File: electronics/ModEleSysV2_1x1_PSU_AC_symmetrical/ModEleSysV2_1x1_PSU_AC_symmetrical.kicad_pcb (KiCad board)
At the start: 2 copper layers, 43.2 x 49.5 mm, 29 parts, among them J2 Jack-DC, SW1 switch_DPDT, U1 LM317, U2 LM337

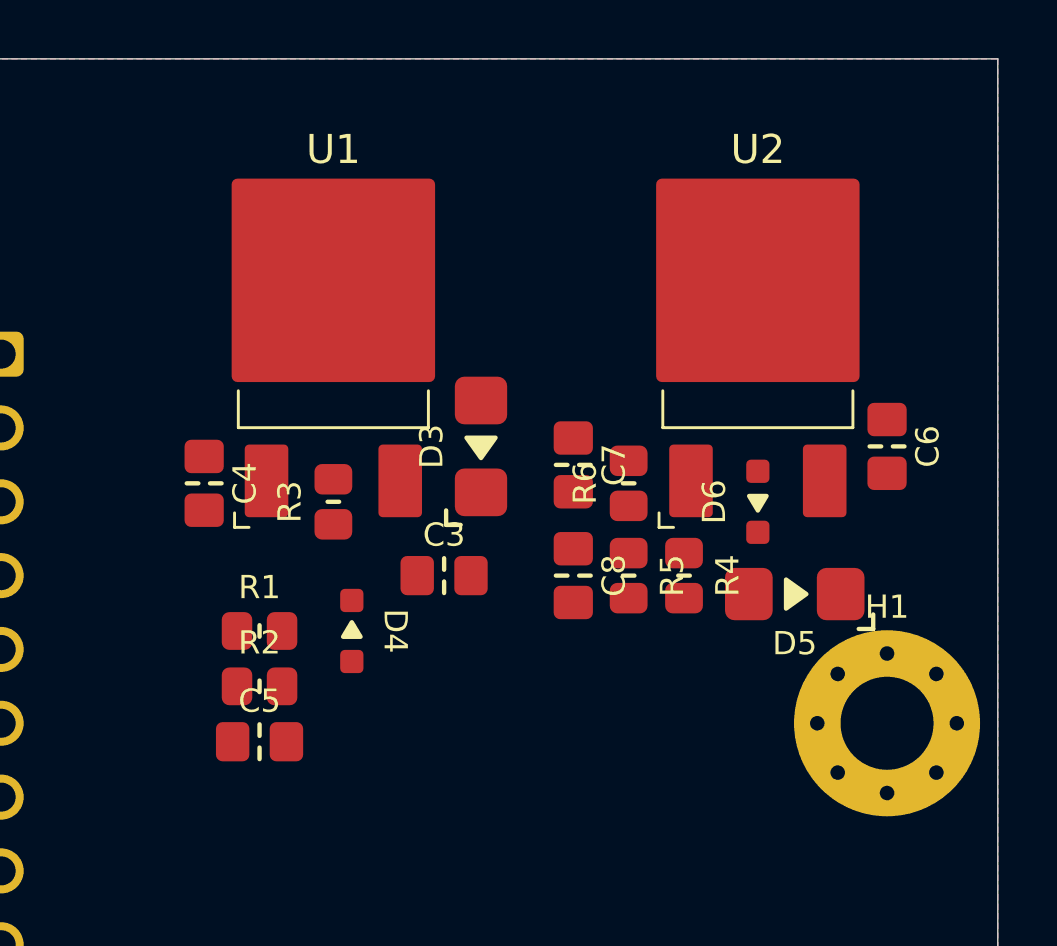
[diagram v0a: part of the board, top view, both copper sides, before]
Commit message: WIP placement of parts and reducing sizes, it is a bit cramped
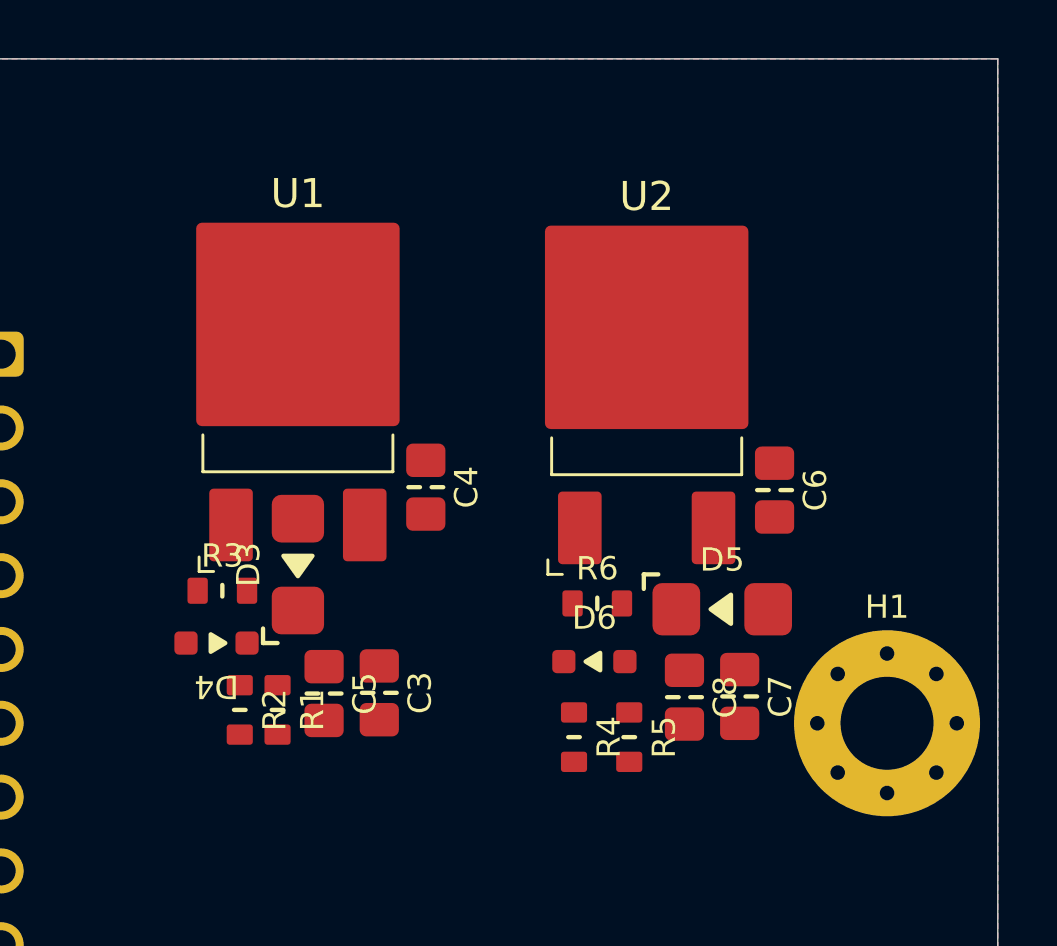
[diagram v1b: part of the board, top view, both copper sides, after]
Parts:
- R1, R2, R3, R4, R5, R6: footprint SquantorResistor:R_0805+0603 -> SquantorResistor:R_0603_hand
- moved C7 9.81 mm to (174.0, 85.4)
- moved D6 7.87 mm to (169.0, 84.2), turned to 0 degrees
- moved C4 7.63 mm to (163.2, 78.2)
- moved D3 7.50 mm to (158.8, 80.9)
- moved R4 6.72 mm to (168.3, 86.8)
- moved C8 5.67 mm to (172.1, 85.5)
- moved R5 5.56 mm to (170.2, 86.8)
- moved R3 4.89 mm to (156.2, 81.8), turned to 0 degrees
- moved D4 4.67 mm to (156.0, 83.6), turned to 180 degrees
- moved C3 4.61 mm to (161.6, 85.3), turned to -90 degrees
- moved R6 4.27 mm to (169.1, 82.2), turned to 0 degrees
- moved U2 4.15 mm to (170.8, 72.7)
- moved C6 4.15 mm to (175.2, 78.3)
- moved R1 2.78 mm to (158.1, 85.9), turned to -90 degrees
- moved C5 2.77 mm to (159.7, 85.3), turned to -90 degrees
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
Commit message: done, needs review in between
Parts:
- added C9: 10n, SquantorCapacitor:C_0805+0603, F.Cu at (150.0, 106.9)
- D1, D2: value D -> A7
- D3, D5: value D -> B5819WS; footprint SquantorDiodes:SOD-123F-hand -> SquantorDiodes:SOD-323HE-shikues
- D4, D6: value D -> B5819WS; footprint SquantorDiodes:SOD-323-nexperia-hand -> SquantorDiodes:SOD-323HE-shikues
- F1: value Fuse -> 0.6A 60V
- R1, R2, R4, R5: value R -> TBD
- moved R4 24.5 mm to (180.2, 65.5), turned to 90 degrees
- moved R5 23.1 mm to (178.9, 65.5), turned to 90 degrees
- moved C8 20.9 mm to (176.5, 65.0), turned to 180 degrees
- moved D6 19.2 mm to (179.0, 67.8), turned to 180 degrees
- moved C7 16.8 mm to (174.1, 68.6), turned to 180 degrees
- moved R6 16.4 mm to (179.5, 69.5), turned to 180 degrees
- moved D5 11.6 mm to (177.1, 71.5), turned to -90 degrees
- moved U2 8.82 mm to (177.1, 78.9), turned to 180 degrees
- moved C3 8.82 mm to (170.4, 85.9)
- moved D4 8.27 mm to (164.0, 85.7)
- moved C4 7.95 mm to (170.4, 81.6)
- moved R3 7.72 mm to (163.6, 84.0)
- moved U1 7.53 mm to (166.0, 74.8)
- moved C5 7.37 mm to (166.9, 86.9), turned to 90 degrees
- moved D3 7.33 mm to (166.0, 82.3)
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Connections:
- net Net-(D4-A) renamed /+adj
- net Net-(D6-K) renamed /-adj
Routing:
- net /+aV: track 0.00 -> 45.2 mm, vias 0 -> 15
- net /-aV: track 0.00 -> 42.8 mm
- net GND: track 0.00 -> 37.3 mm, vias 0 -> 12
- net /DC1n: track 0.00 -> 35.0 mm, vias 0 -> 14
- net /DC1p: track 0.00 -> 29.7 mm
- net /AC_PHASE1_IN: track 0.00 -> 16.4 mm
- net Net-(SW1-SW1_C1): track 0.00 -> 11.4 mm
- net /+adj: track 0.00 -> 10.5 mm
- net /-adj: track 0.00 -> 10.3 mm
- net /AC_NEUT_IN: track 0.00 -> 10.2 mm
- net /AC1_PHASE: track 0.00 -> 8.13 mm
- added copper zone on B.Cu, net /+aV
- added copper zone on F.Cu, net /+aV
- added copper zone on F.Cu, net /-aV
- added copper zone on F.Cu, net /AC1_PHASE
- added copper zone on B.Cu, net /DC1n
- added copper zone on F.Cu, net /DC1n
- added copper zone on F.Cu, net /DC1p

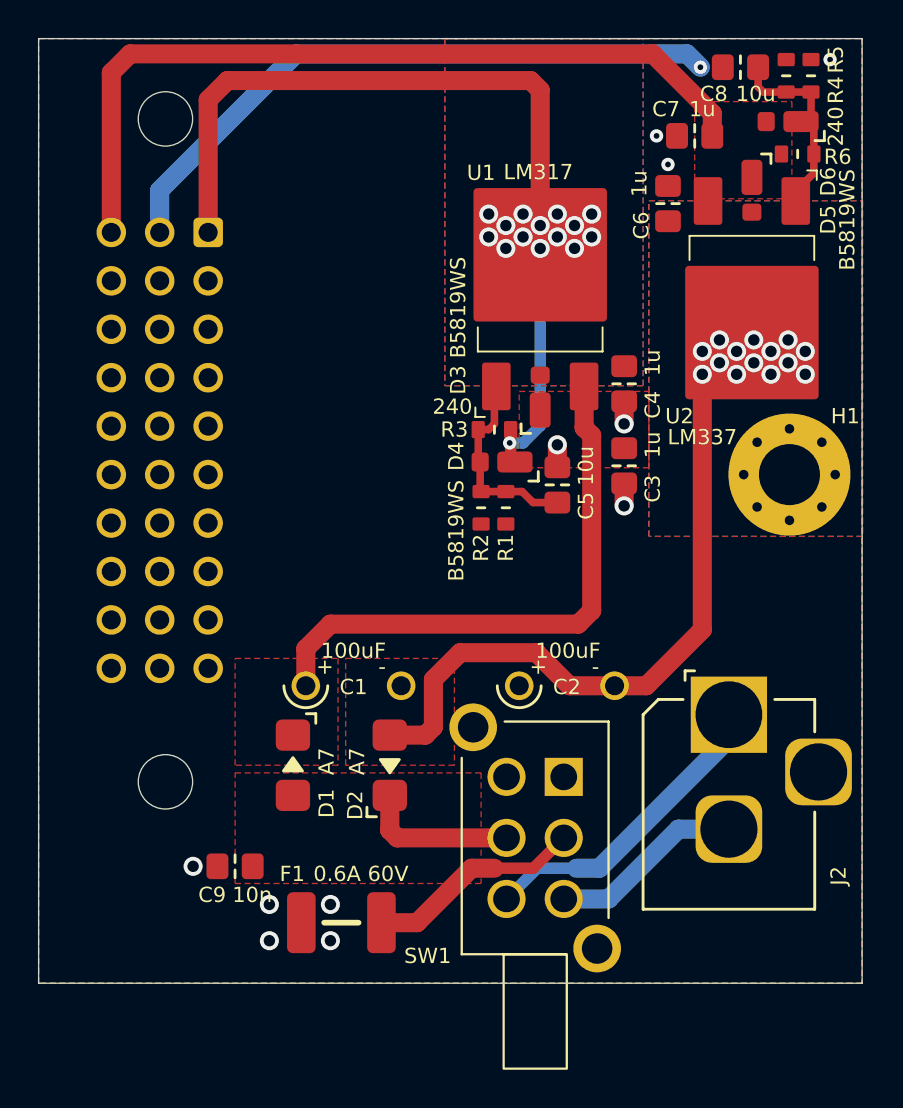
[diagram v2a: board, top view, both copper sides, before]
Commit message: reviewed and different placement of switch and power input
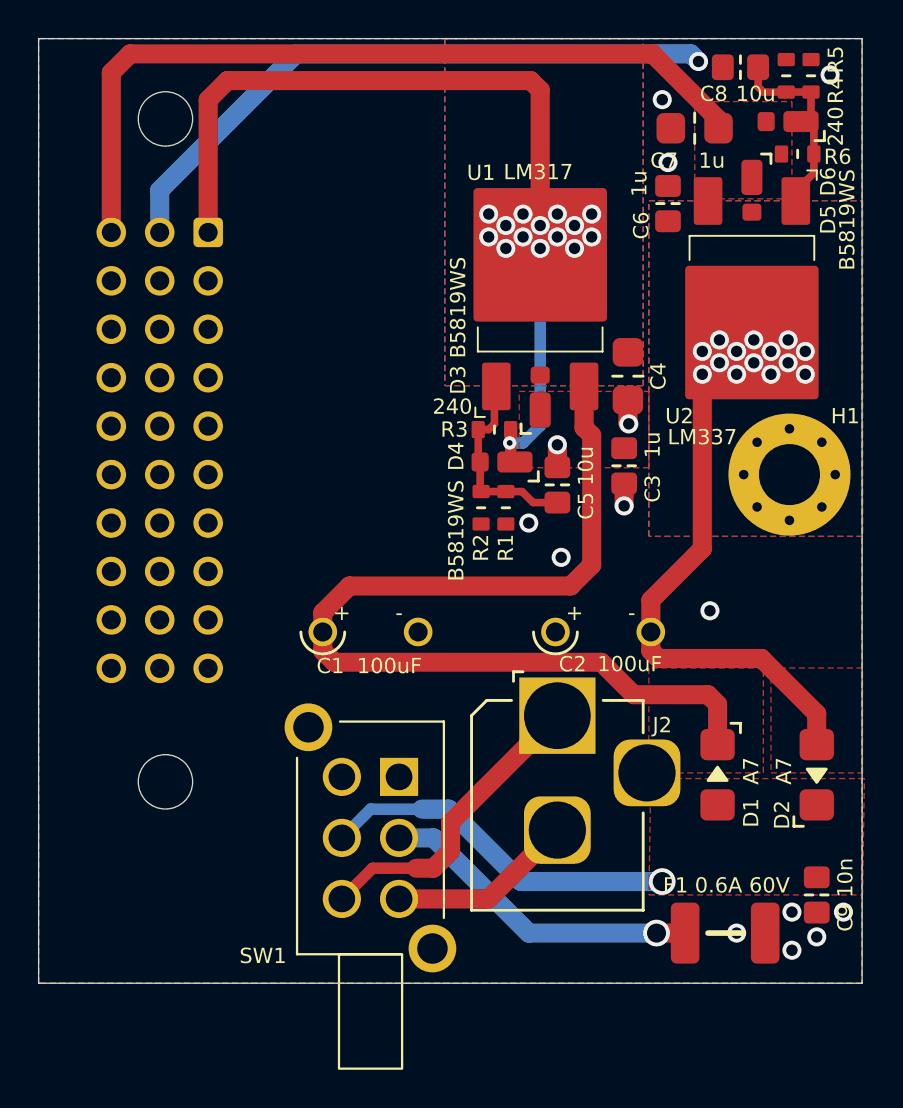
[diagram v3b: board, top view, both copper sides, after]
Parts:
- C4, C7: footprint SquantorCapacitor:C_0805+0603 -> SquantorCapacitor:C_1206_0805
- N1: value 20240311 -> 20240424
- moved C9 30.5 mm to (180.5, 108.4), turned to -90 degrees
- moved N2 27.9 mm to (143.1, 109.2), turned to -90 degrees
- moved D2 22.4 mm to (180.5, 102.1)
- moved N1 22.3 mm to (147.0, 108.6), turned to -90 degrees
- moved D1 22.3 mm to (175.3, 102.1)
- moved F1 20.1 mm to (175.7, 110.4), turned to 0 degrees
- moved J2 9.00 mm to (166.9, 99.0)
- moved SW1 8.64 mm to (157.1, 105.4)
- moved C2 3.40 mm to (169.3, 94.6)
- moved C1 2.96 mm to (157.1, 94.6)
- moved C4 0.45 mm to (170.6, 81.2)
- moved C7 0.40 mm to (174.1, 68.2)
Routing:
- net /DC1p: track 29.7 -> 50.6 mm
- net /AC1_PHASE: track 8.13 -> 19.0 mm, vias 0 -> 1
- net /DC1n: track 35.0 -> 27.3 mm
- net Net-(SW1-SW1_C1): track 11.4 -> 17.1 mm, vias 0 -> 1
- net GND: track 37.3 -> 37.2 mm, vias 12 -> 15

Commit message: updated versionnumbers
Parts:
- N1: value 20240424 -> 20240426
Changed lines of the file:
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@@
         (effects (font (size 1 1) (thickness 0.15)) (justify mirror))
     )
-    (fp_text value "20240424" (at 0.8 0.1 -270) (layer "B.SilkS")
+    (fp_text value "20240426" (at 0.8 0.1 -270) (layer "B.SilkS")
         (effects (font (size 0.8 0.8) (thickness 0.15)) (justify mirror))
     )
